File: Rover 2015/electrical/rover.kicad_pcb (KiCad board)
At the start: 2 copper layers, 24 parts, among them Q1 TIP120, Q2 TIP120, Q3 TIP120

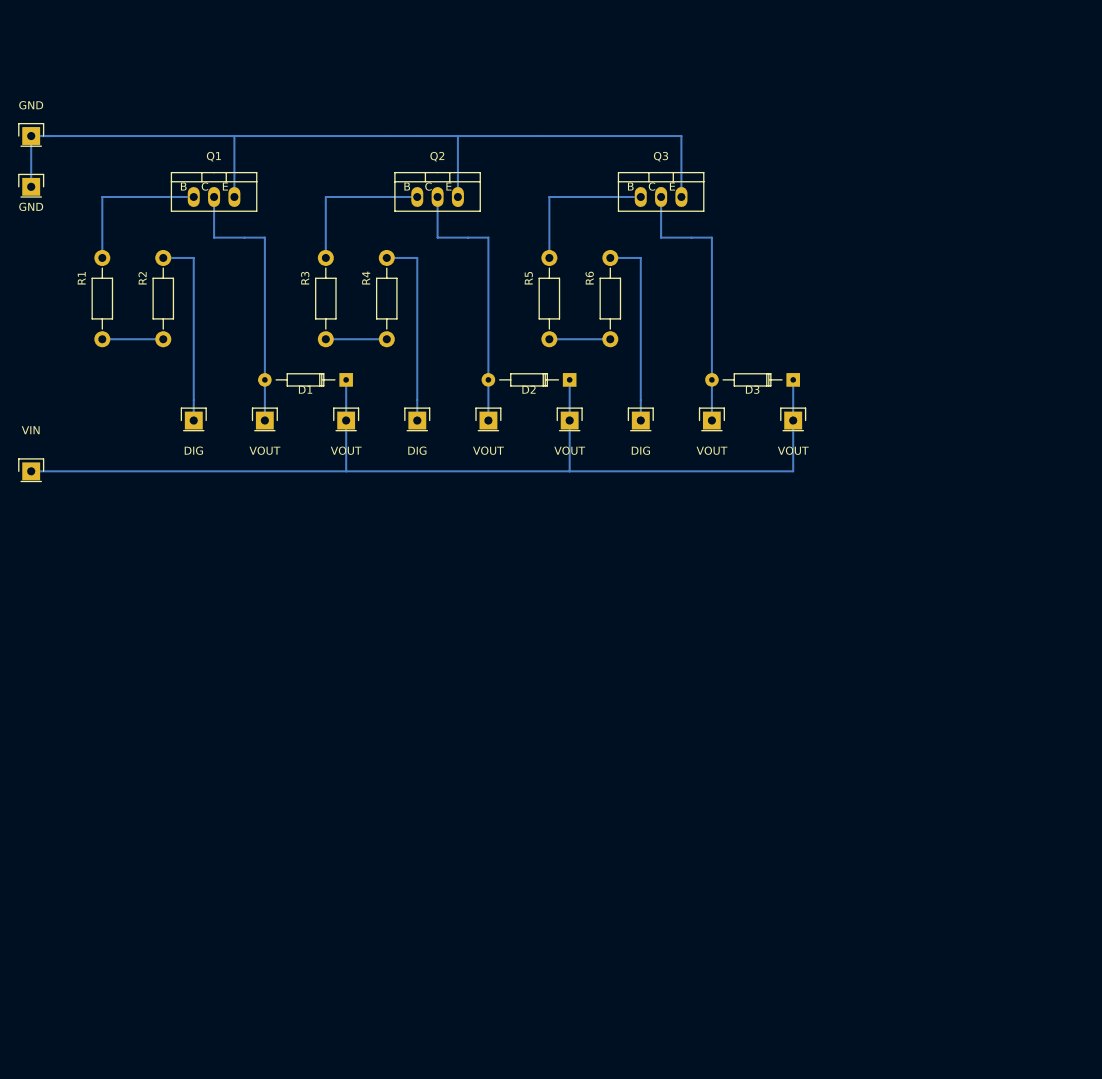
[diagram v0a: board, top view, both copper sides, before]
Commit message: Add larger trace widths to Solenoid Driver Board.  Add power distribution board.
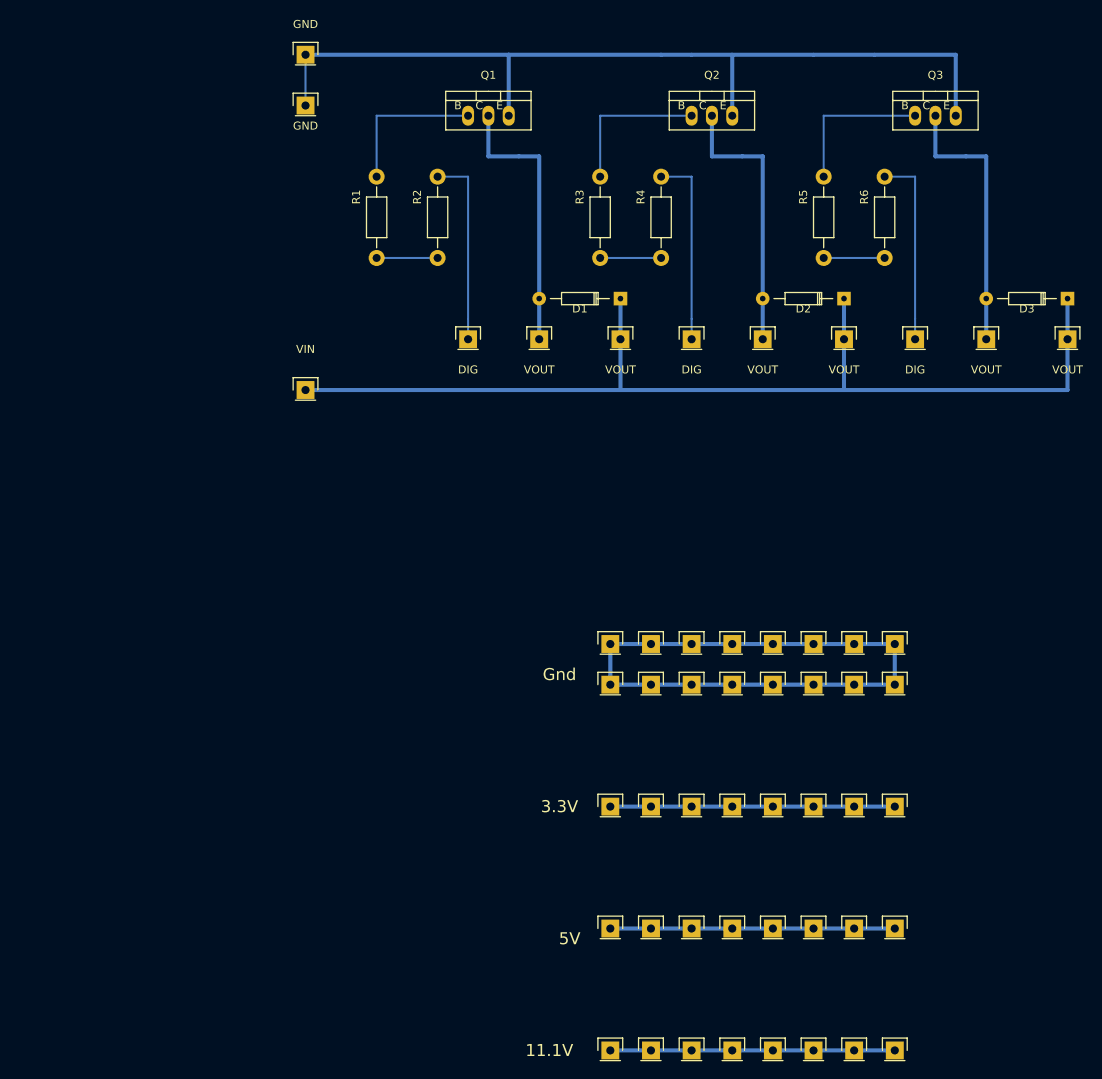
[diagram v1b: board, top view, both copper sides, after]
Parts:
- added ?: , Pin_Headers:Pin_Header_Straight_1x01, F.Cu at (91.4, 142.2)
- added ?: , Pin_Headers:Pin_Header_Straight_1x01, F.Cu at (116.8, 127.0)
- added ?: , Pin_Headers:Pin_Header_Straight_1x01, F.Cu at (127.0, 127.0)
- added ?: , Pin_Headers:Pin_Header_Straight_1x01, F.Cu at (121.9, 127.0)
- added ?: , Pin_Headers:Pin_Header_Straight_1x01, F.Cu at (101.6, 127.0)
- added ?: , Pin_Headers:Pin_Header_Straight_1x01, F.Cu at (106.7, 127.0)
- added ?: , Pin_Headers:Pin_Header_Straight_1x01, F.Cu at (96.5, 127.0)
- added ?: , Pin_Headers:Pin_Header_Straight_1x01, F.Cu at (91.4, 127.0)
- added ?: , Pin_Headers:Pin_Header_Straight_1x01, F.Cu at (91.4, 157.5)
- added ?: , Pin_Headers:Pin_Header_Straight_1x01, F.Cu at (96.5, 157.5)
- added ?: , Pin_Headers:Pin_Header_Straight_1x01, F.Cu at (106.7, 157.5)
- added ?: , Pin_Headers:Pin_Header_Straight_1x01, F.Cu at (96.5, 142.2)
- added ?: , Pin_Headers:Pin_Header_Straight_1x01, F.Cu at (101.6, 157.5)
- added ?: , Pin_Headers:Pin_Header_Straight_1x01, F.Cu at (121.9, 157.5)
- added ?: , Pin_Headers:Pin_Header_Straight_1x01, F.Cu at (127.0, 157.5)
- added ?: , Pin_Headers:Pin_Header_Straight_1x01, F.Cu at (116.8, 157.5)
- added ?: , Pin_Headers:Pin_Header_Straight_1x01, F.Cu at (111.8, 157.5)
- added ?: , Pin_Headers:Pin_Header_Straight_1x01, F.Cu at (91.4, 111.8)
- added ?: , Pin_Headers:Pin_Header_Straight_1x01, F.Cu at (96.5, 111.8)
- added ?: , Pin_Headers:Pin_Header_Straight_1x01, F.Cu at (106.7, 111.8)
- added ?: , Pin_Headers:Pin_Header_Straight_1x01, F.Cu at (101.6, 111.8)
- added ?: , Pin_Headers:Pin_Header_Straight_1x01, F.Cu at (121.9, 111.8)
- added ?: , Pin_Headers:Pin_Header_Straight_1x01, F.Cu at (106.7, 142.2)
- added ?: , Pin_Headers:Pin_Header_Straight_1x01, F.Cu at (127.0, 111.8)
- added ?: , Pin_Headers:Pin_Header_Straight_1x01, F.Cu at (116.8, 111.8)
- added ?: , Pin_Headers:Pin_Header_Straight_1x01, F.Cu at (111.8, 111.8)
- added ?: , Pin_Headers:Pin_Header_Straight_1x01, F.Cu at (111.8, 106.7)
- added ?: , Pin_Headers:Pin_Header_Straight_1x01, F.Cu at (116.8, 106.7)
- added ?: , Pin_Headers:Pin_Header_Straight_1x01, F.Cu at (127.0, 106.7)
- added ?: , Pin_Headers:Pin_Header_Straight_1x01, F.Cu at (121.9, 106.7)
- added ?: , Pin_Headers:Pin_Header_Straight_1x01, F.Cu at (101.6, 106.7)
- added ?: , Pin_Headers:Pin_Header_Straight_1x01, F.Cu at (106.7, 106.7)
- added ?: , Pin_Headers:Pin_Header_Straight_1x01, F.Cu at (96.5, 106.7)
- added ?: , Pin_Headers:Pin_Header_Straight_1x01, F.Cu at (101.6, 142.2)
- added ?: , Pin_Headers:Pin_Header_Straight_1x01, F.Cu at (91.4, 106.7)
- added ?: , Pin_Headers:Pin_Header_Straight_1x01, F.Cu at (121.9, 142.2)
- added ?: , Pin_Headers:Pin_Header_Straight_1x01, F.Cu at (127.0, 142.2)
- added ?: , Pin_Headers:Pin_Header_Straight_1x01, F.Cu at (116.8, 142.2)
- added ?: , Pin_Headers:Pin_Header_Straight_1x01, F.Cu at (111.8, 142.2)
- added ?: , Pin_Headers:Pin_Header_Straight_1x01, F.Cu at (111.8, 127.0)
- moved GND 35.8 mm to (53.3, 33.0)
- moved GND 35.8 mm to (53.3, 39.4)
- moved Q1 35.8 mm to (76.2, 40.6)
- moved Q2 35.8 mm to (104.1, 40.6)
- moved Q3 35.8 mm to (132.1, 40.6)
- moved R4 35.8 mm to (97.8, 53.3)
- moved R5 35.8 mm to (118.1, 53.3)
- moved R6 35.8 mm to (125.7, 53.3)
- moved VIN 35.8 mm to (53.3, 74.9)
- moved VOUT 35.8 mm to (138.4, 68.6)
- moved VOUT 35.8 mm to (148.6, 68.6)
- moved VOUT 35.8 mm to (120.7, 68.6)
- moved DIG 35.8 mm to (73.7, 68.6)
- moved R3 35.8 mm to (90.2, 53.3)
- moved VOUT 35.8 mm to (82.5, 68.6)
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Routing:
- net (no net): track 496.6 -> 690.9 mm
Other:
- board text added: "11.1V"
- board text added: "3.3V"
- board text added: "5V"
- board text added: "Gnd"
- board text added: "Power Distribution Board"
- board text added: "Solenoid Driver Board"
